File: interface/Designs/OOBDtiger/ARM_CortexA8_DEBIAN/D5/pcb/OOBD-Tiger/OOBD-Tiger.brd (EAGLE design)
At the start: 63.4 x 38.2 mm, 122 parts, among them IC1 ADM3053M, IC2 ADM3053M, IC4 DS3231, U1 SY6280, U10 MP1482DS, U2 SN65HVD230(SO8), U3 SY6280, U6 SN65HVD230(SO8)

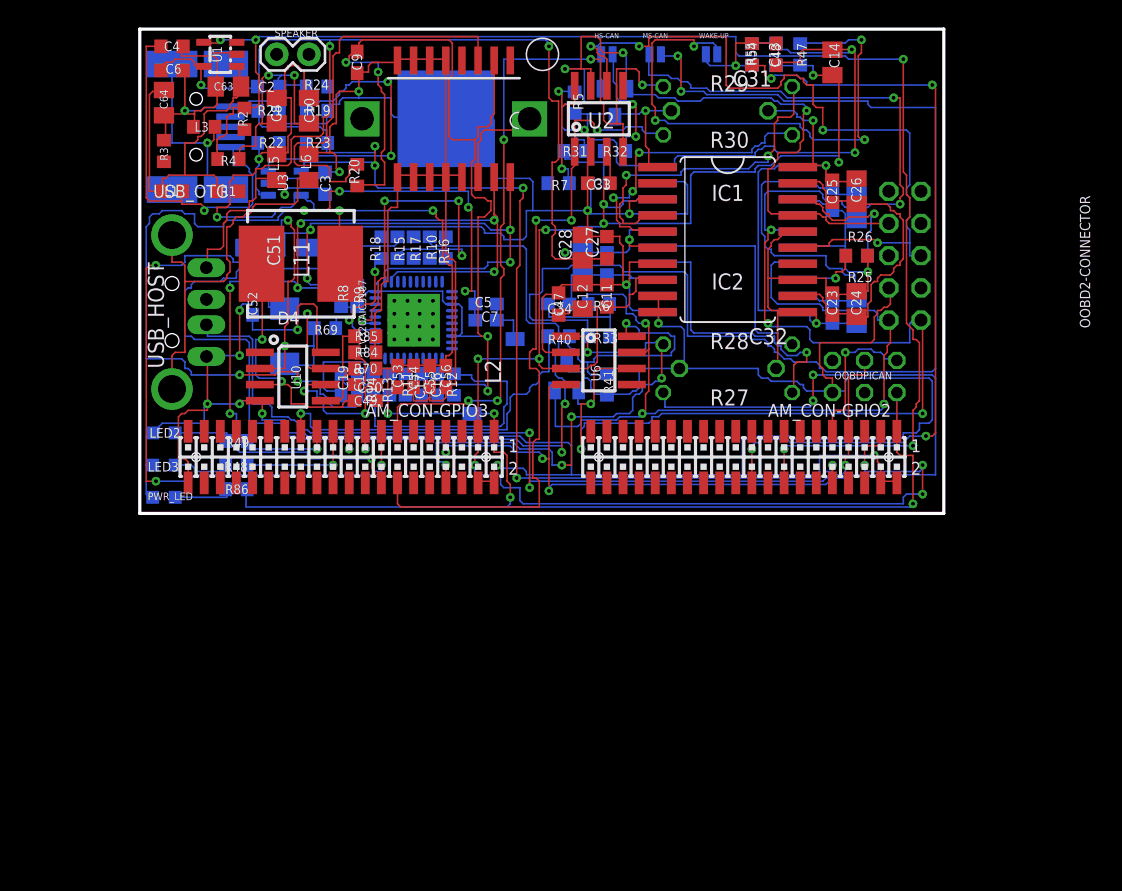
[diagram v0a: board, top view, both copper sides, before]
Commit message: Letzter Stand, Endplaziert,Teilweise gerouted.
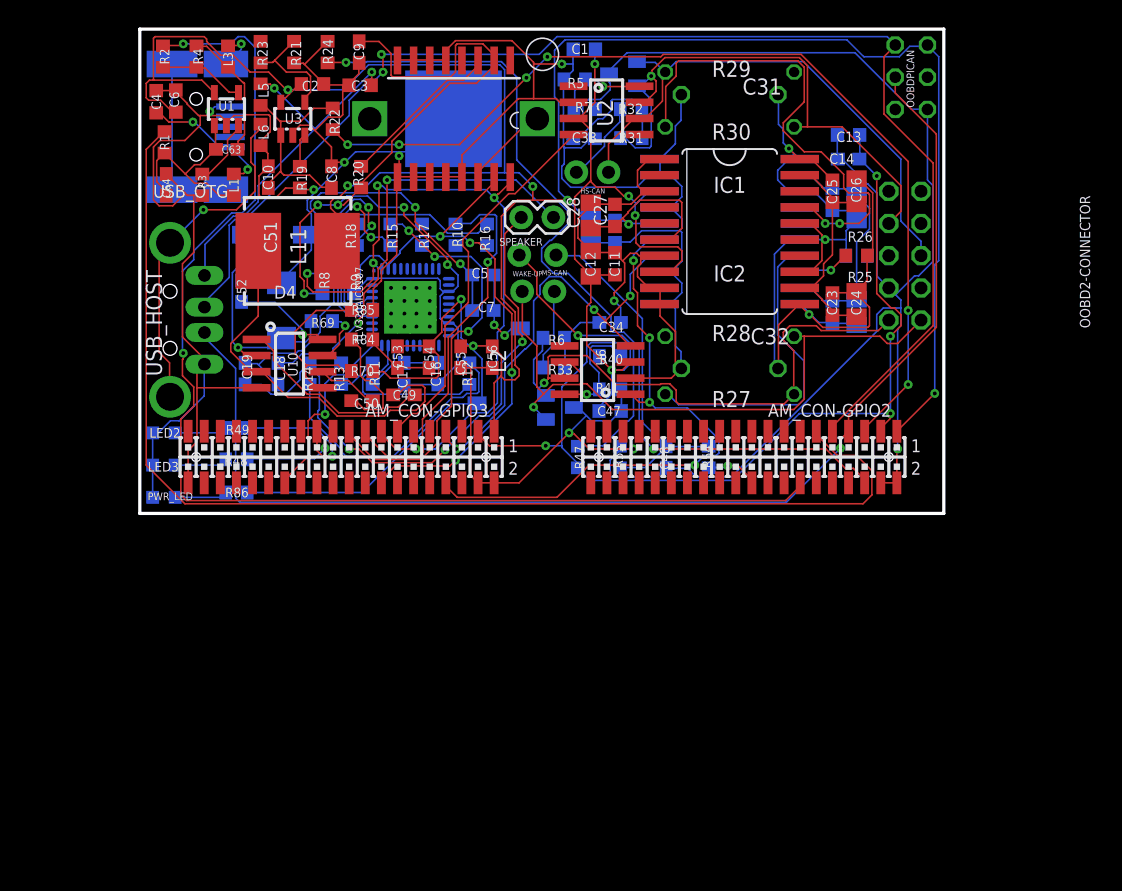
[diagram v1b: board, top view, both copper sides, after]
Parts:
- C10, C14, C63, C64, C8: device rcl:C0805K -> rcl:C0603
- HS-CAN, MS-CAN: device SparkFun:SJ_2S-NO -> SparkFun:1X02
- L5, L6: device rcl:L0805_5MIL_DWS -> rcl:L0603
- WAKE-UP: device SparkFun:SJ_2S-NO -> SparkFun:1X02_LOCK
- moved R47 36.3 mm to (34.5, 4.45)
- moved R55 33.4 mm to (37.8, 4.45)
- moved C48 32.9 mm to (41.5, 4.45), flipped to the bottom
- moved R54 31.9 mm to (44.9, 4.45), flipped to the bottom
- moved OOBDPICAN 23.9 mm to (60.8, 34.4), turned to 270 degrees
- moved WAKE-UP 21.8 mm to (30.1, 20.4), turned to 180 degrees
- moved SPEAKER 21.1 mm to (30.1, 23.3), turned to 0 degrees
- moved MS-CAN 20.3 mm to (32.7, 17.5)
- moved C1 10.6 mm to (35.1, 36.6), flipped to the bottom, turned to 0 degrees
- moved HS-CAN 9.60 mm to (34.4, 26.9), turned to 180 degrees
- moved C47 9.36 mm to (37.1, 8.08), flipped to the bottom, turned to 180 degrees
- moved C13 8.54 mm to (55.9, 29.8), turned to 0 degrees
- moved R4 8.46 mm to (4.47, 36.0), turned to 270 degrees
- moved R23 8.43 mm to (9.53, 36.4), flipped to the top, turned to 90 degrees
- moved C3 8.20 mm to (17.4, 33.8), flipped to the top, turned to 180 degrees
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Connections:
- removed net N$39: IC1.4, R29.1
- removed net N$41: IC1.5, R30.1
- new net N$12: IC2.17, R27.2
- new net N$36: IC1.15, R29.1
- new net N$37: IC1.5
- new net N$38: IC1.4
- net CAN0_H: now also R27.1; no longer IC2.17
- net CAN0_L: now also R28.1; no longer IC2.15
- net CAN1_H: now also R30.1; no longer IC1.17
- net CAN1_L: now also R29.2; no longer IC1.15
- net DCAN0_RX: now also IC2.4; no longer R27.2
- net DCAN0_TX: now also IC2.5; no longer R28.2
- net DCAN1_RX: no longer R29.2
- net DCAN1_TX: no longer R30.2
- net N$34: now also IC2.15, R28.2; no longer IC2.4, R27.1
- net N$35: now also IC1.17, R30.2; no longer IC2.5, R28.1
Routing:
- net USB0_DRV: track 113.8 -> 6.79 mm, vias 5 -> 0
- net USB0_CE: track 0.00 -> 96.6 mm, vias 0 -> 2
- net USB0_VBUS: track 0.00 -> 93.4 mm
- net USB1_DM: track 11.9 -> 103.7 mm, vias 1 -> 2
- net N$32: track 94.4 -> 6.37 mm, vias 2 -> 0
- net USB1_DRV: track 84.2 -> 8.95 mm, vias 5 -> 0
- net USB1_VBUS: track 0.00 -> 75.0 mm, vias 0 -> 6
- net USB1_ID: track 0.00 -> 70.1 mm, vias 0 -> 2
- net CAN0_L: track 119.5 -> 52.0 mm, vias 7 -> 1
- net GND: track 509.0 -> 451.5 mm, vias 20 -> 9
- net EXT_WAKEUP: track 61.3 -> 4.16 mm, vias 4 -> 1
- net DCAN1_TX: track 56.0 -> 0.00 mm, vias 3 -> 0
- net DCAN0_RX: track 84.4 -> 34.7 mm, vias 5 -> 3
- net I2C0-SCL: track 96.4 -> 56.4 mm, vias 7 -> 5
- net N$14: track 8.15 -> 45.9 mm, vias 0 -> 3
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
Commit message: minor changes on CAN interfaces and start component placing improvement
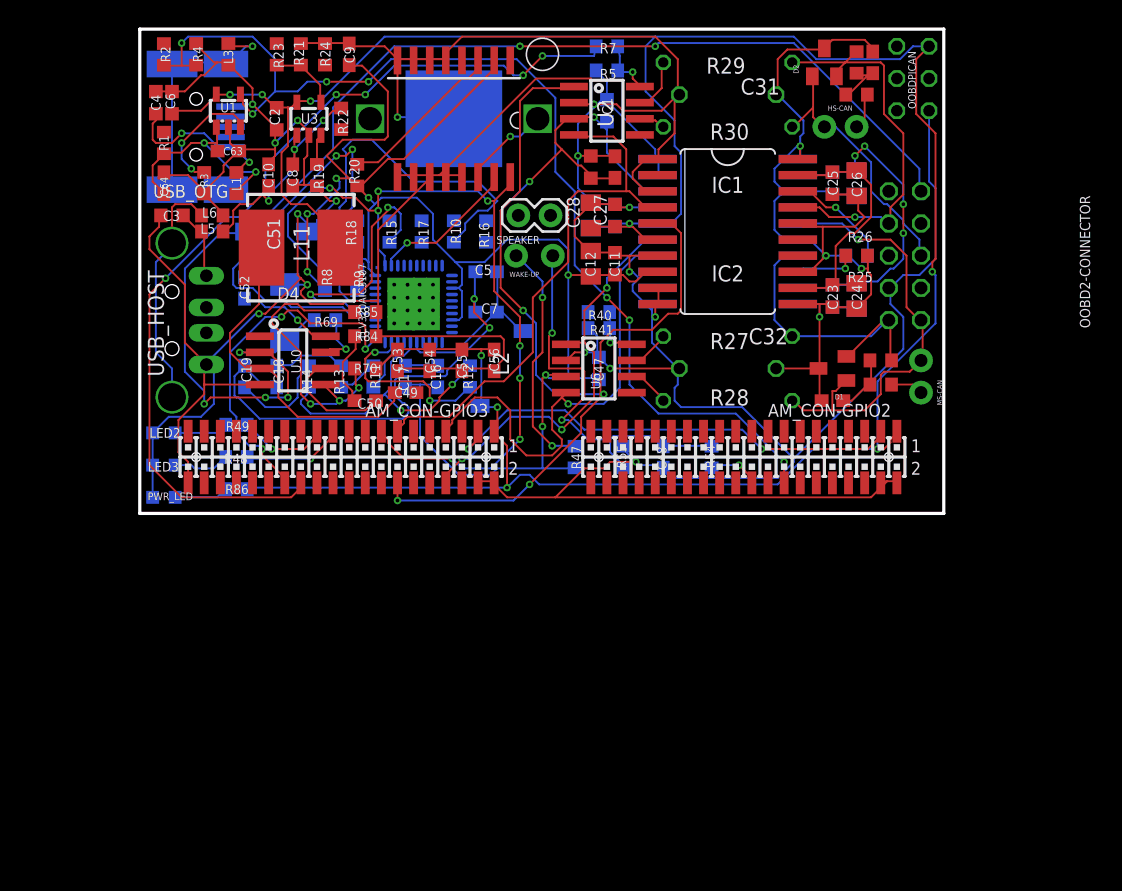
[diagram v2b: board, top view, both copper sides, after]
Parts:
- R27, R28, R29, R30: value NA (0R) -> 0R
- moved MS-CAN 30.0 mm to (61.6, 9.53), turned to 90 degrees
- moved R6 25.8 mm to (58.4, 12.1), flipped to the top
- moved R33 25.8 mm to (58.4, 10.2), flipped to the top
- moved C33 23.5 mm to (57.8, 35.6), flipped to the top, turned to 90 degrees
- moved HS-CAN 22.4 mm to (56.5, 30.5), turned to 0 degrees
- moved D1 21.7 mm to (54.6, 11.4), flipped to the top
- moved C13 20.5 mm to (35.6, 27.3), flipped to the top, turned to 90 degrees
- moved R31 18.7 mm to (56.5, 35.6), flipped to the top, turned to 90 degrees
- moved C34 18.6 mm to (54.6, 8.89), flipped to the top
- moved C14 18.4 mm to (37.5, 27.3), flipped to the top, turned to 90 degrees
- moved C3 18.0 mm to (2.54, 23.5)
- moved R32 17.8 mm to (56.5, 33.0), flipped to the top
- moved D2 15.9 mm to (54.0, 35.6), flipped to the top, turned to 0 degrees
- moved L5 11.4 mm to (5.71, 22.2), turned to 180 degrees
- moved L6 7.41 mm to (5.71, 23.5), turned to 180 degrees
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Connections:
- removed net N$12: IC2.17, R27.2
- removed net N$34: IC2.15, R28.2
- removed net N$35: IC1.17, R30.2
- removed net N$36: IC1.15, R29.1
- removed net N$37: IC1.5
- removed net N$38: IC1.4
- new net N$40: R27.2, U6.7
- new net N$41: R30.2, U2.6
- new net N$42: R28.2, U6.6
- new net N$45: R29.1, U2.7
- net +3V3: now also C1.1, C11.1, C12.1, C13.1, C14.1, C47.1, IC1.8, IC2.8, R47.2, U2.3, U6.3
- net 3V3: no longer C1.1, C11.1, C12.1, C13.1, C14.1, C47.1, IC1.8, IC2.8, R47.2, U2.3, U6.3
- net CAN0_H: now also IC2.17; no longer U6.7
- net CAN0_L: now also IC2.15; no longer U6.6
- net CAN1_H: now also IC1.17, R29.2; no longer R30.1, U2.7
- net CAN1_L: now also IC1.15, R30.1; no longer R29.2, U2.6
- net DCAN1_RX: now also IC1.4
- net DCAN1_TX: now also IC1.5
- net GND: no longer C33.2, C34.2, D1.3, D2.3
- net GNDA: now also C33.2, C34.2, D1.3, D2.3
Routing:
- net USB1_DM: track 103.7 -> 0.00 mm, vias 2 -> 0
- net USB1_DP: track 97.4 -> 0.00 mm, vias 1 -> 0
- net USB0_CE: track 96.6 -> 0.00 mm, vias 2 -> 0
- net USB0_VBUS: track 93.4 -> 0.00 mm
- net 3V3: track 130.6 -> 37.6 mm, vias 8 -> 2
- net +12V: track 19.1 -> 105.5 mm, vias 1 -> 6
- net +3V3: track 80.3 -> 163.5 mm, vias 5 -> 9
- net USB0_DRV: track 6.79 -> 85.5 mm, vias 0 -> 7
- net DCAN1_TX: track 0.00 -> 75.8 mm, vias 0 -> 4
- net USB1_VBUS: track 75.0 -> 0.00 mm, vias 6 -> 0
- net HS-CAN_RS: track 0.00 -> 72.6 mm, vias 0 -> 5
- net USB1_ID: track 70.1 -> 0.00 mm, vias 2 -> 0
- net N$35: track 38.9 -> 0.00 mm, vias 2 -> 0
- net N$14: track 45.9 -> 8.00 mm, vias 3 -> 0
- net N$25: track 0.00 -> 34.2 mm
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
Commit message: further improvement on component placing (94,2% autotrouter) now!
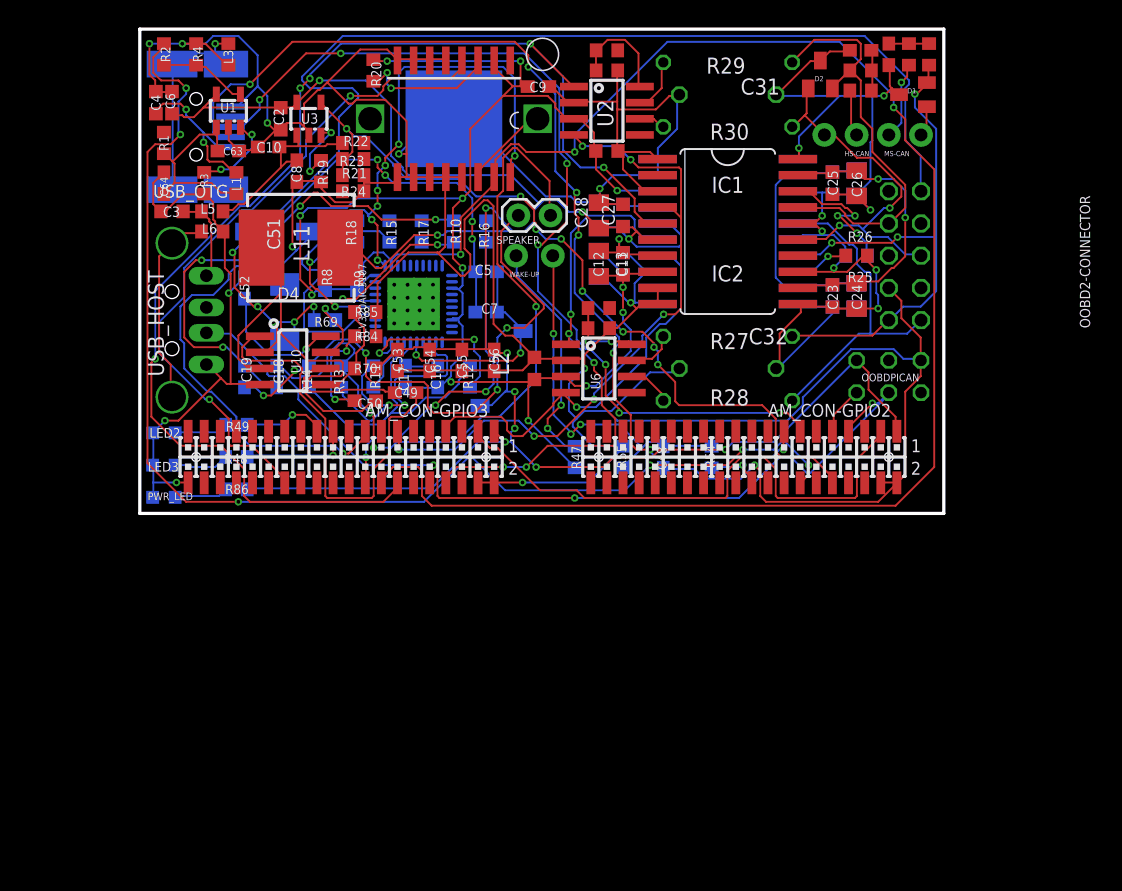
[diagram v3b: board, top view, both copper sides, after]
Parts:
- C14: device rcl:C0603 -> rcl:C0805K
- moved C34 27.7 mm to (59.1, 36.2), turned to 270 degrees
- moved R33 26.1 mm to (60.6, 36.2), turned to 270 degrees
- moved R6 24.4 mm to (62.2, 36.2), turned to 270 degrees
- moved OOBDPICAN 23.6 mm to (59.1, 10.8), turned to 180 degrees
- moved D1 22.5 mm to (61.0, 33.0)
- moved MS-CAN 20.5 mm to (59.1, 29.8), turned to 180 degrees
- moved C9 15.1 mm to (31.4, 33.7), turned to 180 degrees
- moved R24 11.0 mm to (16.8, 25.4), turned to 180 degrees
- moved R21 10.4 mm to (16.8, 26.7), turned to 180 degrees
- moved R23 10.2 mm to (16.8, 27.9), turned to 0 degrees
- moved R20 8.35 mm to (18.4, 34.9), turned to 90 degrees
- moved C13 8.03 mm to (38.1, 19.7), flipped to the bottom
- moved C14 7.73 mm to (36.2, 19.7), flipped to the bottom, turned to 270 degrees
- moved C47 5.08 mm to (31.1, 11.4), flipped to the top
- moved C1 3.18 mm to (36.8, 28.6), flipped to the top, turned to 0 degrees
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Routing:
- net I2C0-SDA: track 11.7 -> 135.5 mm, vias 1 -> 3
- net USB0_CE: track 0.00 -> 97.4 mm, vias 0 -> 6
- net USB0_DM: track 0.00 -> 80.2 mm, vias 0 -> 7
- net USB0_DRV: track 85.5 -> 6.99 mm, vias 7 -> 0
- net USB0_DP: track 0.00 -> 74.9 mm, vias 0 -> 7
- net HS-CAN_RS: track 72.6 -> 0.00 mm, vias 5 -> 0
- net USB1_DP: track 0.00 -> 70.3 mm, vias 0 -> 3
- net USB1_DRV: track 5.53 -> 63.2 mm, vias 0 -> 8
- net N$15: track 5.72 -> 59.5 mm, vias 0 -> 3
- net AUD_WCLK: track 0.00 -> 51.0 mm, vias 0 -> 3
- net +5V: track 220.2 -> 177.4 mm, vias 9 -> 11
- net N$14: track 8.00 -> 45.4 mm, vias 0 -> 5
- net N$7: track 0.00 -> 32.6 mm
- net GND: track 430.2 -> 397.7 mm, vias 16 -> 14
- net +3V3: track 163.5 -> 131.5 mm, vias 9 -> 12
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
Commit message: further optimization of component placing (now 97,3%) => only audio chip is lacking due to missing power supply connections and missing 1V8 LDO :-(
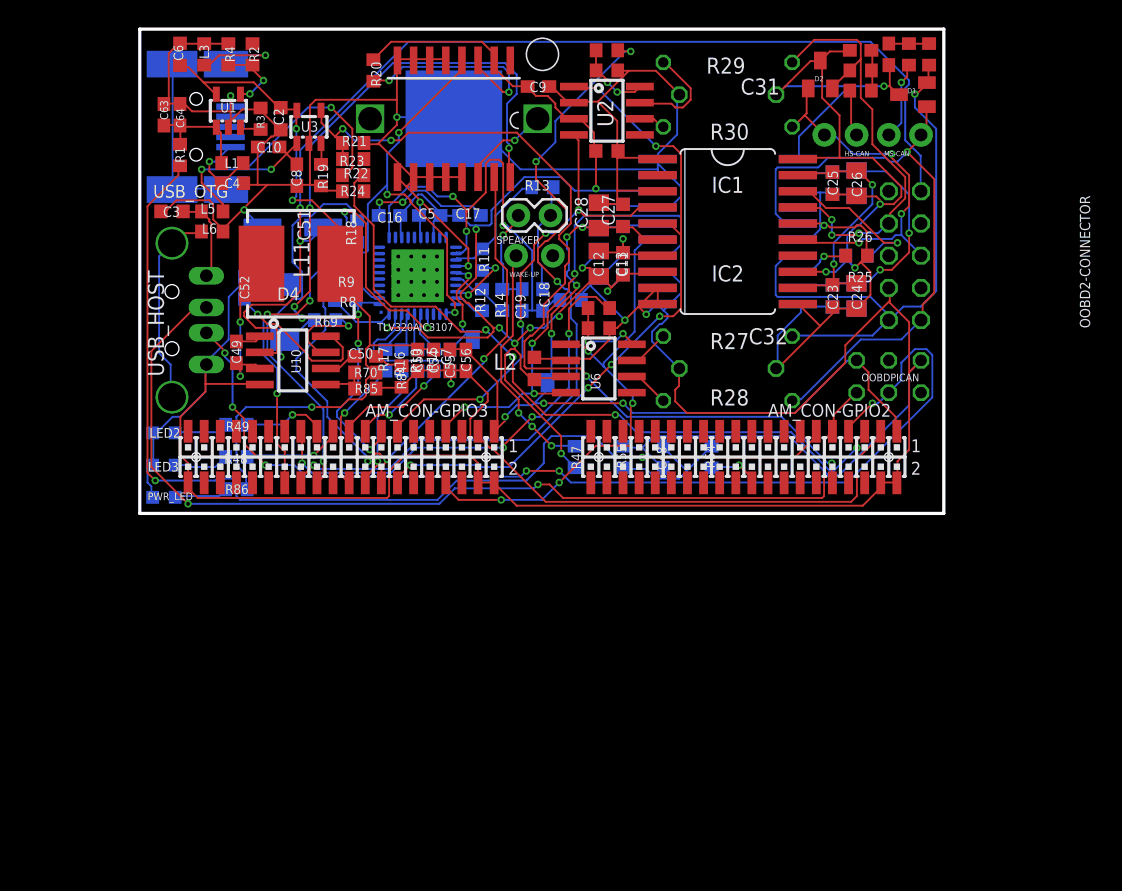
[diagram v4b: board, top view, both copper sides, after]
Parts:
- added L4: FB0805/600R/2A, rcl:L0603
- moved C19 22.7 mm to (30.2, 16.8), turned to 90 degrees
- moved C18 21.8 mm to (31.8, 16.8)
- moved R13 21.8 mm to (31.8, 25.7), turned to 180 degrees
- moved R14 16.4 mm to (28.6, 16.8)
- moved C49 13.7 mm to (7.62, 12.7), turned to 270 degrees
- moved C17 13.7 mm to (26.0, 23.5), turned to 180 degrees
- moved C16 13.3 mm to (19.7, 23.5), turned to 0 degrees
- moved R11 12.6 mm to (27.0, 20.0)
- moved R16 12.2 mm to (20.6, 12.1)
- moved R15 10.7 mm to (23.2, 12.1), turned to 90 degrees
- moved R10 10.6 mm to (21.9, 12.1), turned to 90 degrees
- moved R17 10.6 mm to (19.4, 12.1), turned to 90 degrees
- moved C4 8.76 mm to (7.30, 26.0), turned to 0 degrees
- moved R2 6.99 mm to (8.89, 36.2)
- moved R3 6.75 mm to (9.53, 31.1), turned to 270 degrees
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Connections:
- net +3V3: now also C5.2
- net AGND: now also L4.2, TLV320AIC3107.11, TLV320AIC3107.22; no longer C5.1, C7.1
- net GND: now also C5.1, C7.1, L4.1, TLV320AIC3107.16, TLV320AIC3107.24, TLV320AIC3107.39
- net N$17: no longer C5.2
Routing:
- net USB0_CE: track 97.4 -> 0.00 mm, vias 6 -> 0
- net USB0_VBUS: track 0.00 -> 84.4 mm, vias 0 -> 2
- net I2C0-SDA: track 135.5 -> 54.2 mm
- net USB0_DM: track 80.2 -> 0.00 mm, vias 7 -> 0
- net USB1_DM: track 3.87 -> 79.5 mm, vias 0 -> 2
- net USB0_DP: track 74.9 -> 0.00 mm, vias 7 -> 0
- net HS-CAN_RS: track 0.00 -> 59.9 mm, vias 0 -> 4
- net USB1_VBUS: track 0.00 -> 57.7 mm, vias 0 -> 4
- net N$15: track 59.5 -> 8.74 mm, vias 3 -> 0
- net DCAN1_TX: track 100.0 -> 53.5 mm, vias 5 -> 6
- net AUD_WCLK: track 51.0 -> 6.99 mm, vias 3 -> 1
- net +5V: track 177.4 -> 139.7 mm, vias 11 -> 10
- net N$14: track 45.4 -> 8.15 mm, vias 5 -> 1
- net MS-CAN_RS: track 0.00 -> 37.0 mm, vias 0 -> 4
- net AUD_MCLK: track 0.00 -> 30.8 mm, vias 0 -> 1
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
